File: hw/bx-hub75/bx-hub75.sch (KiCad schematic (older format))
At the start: 8 parts, among them U1 74HCT244, U2 74HCT244

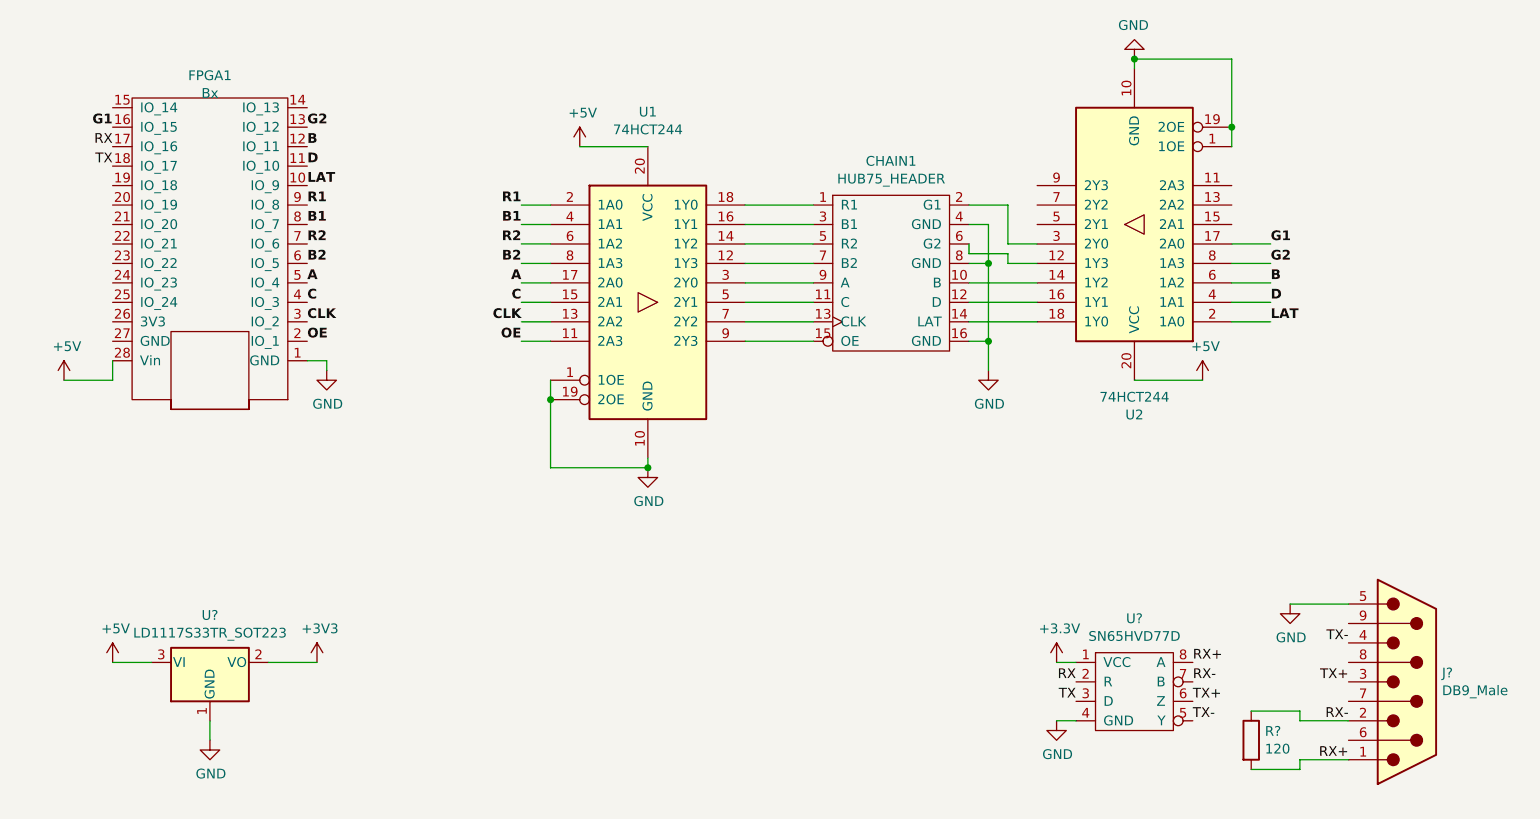
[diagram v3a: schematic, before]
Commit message: hw/bx-hub75: add SPI eeprom/decoupling caps
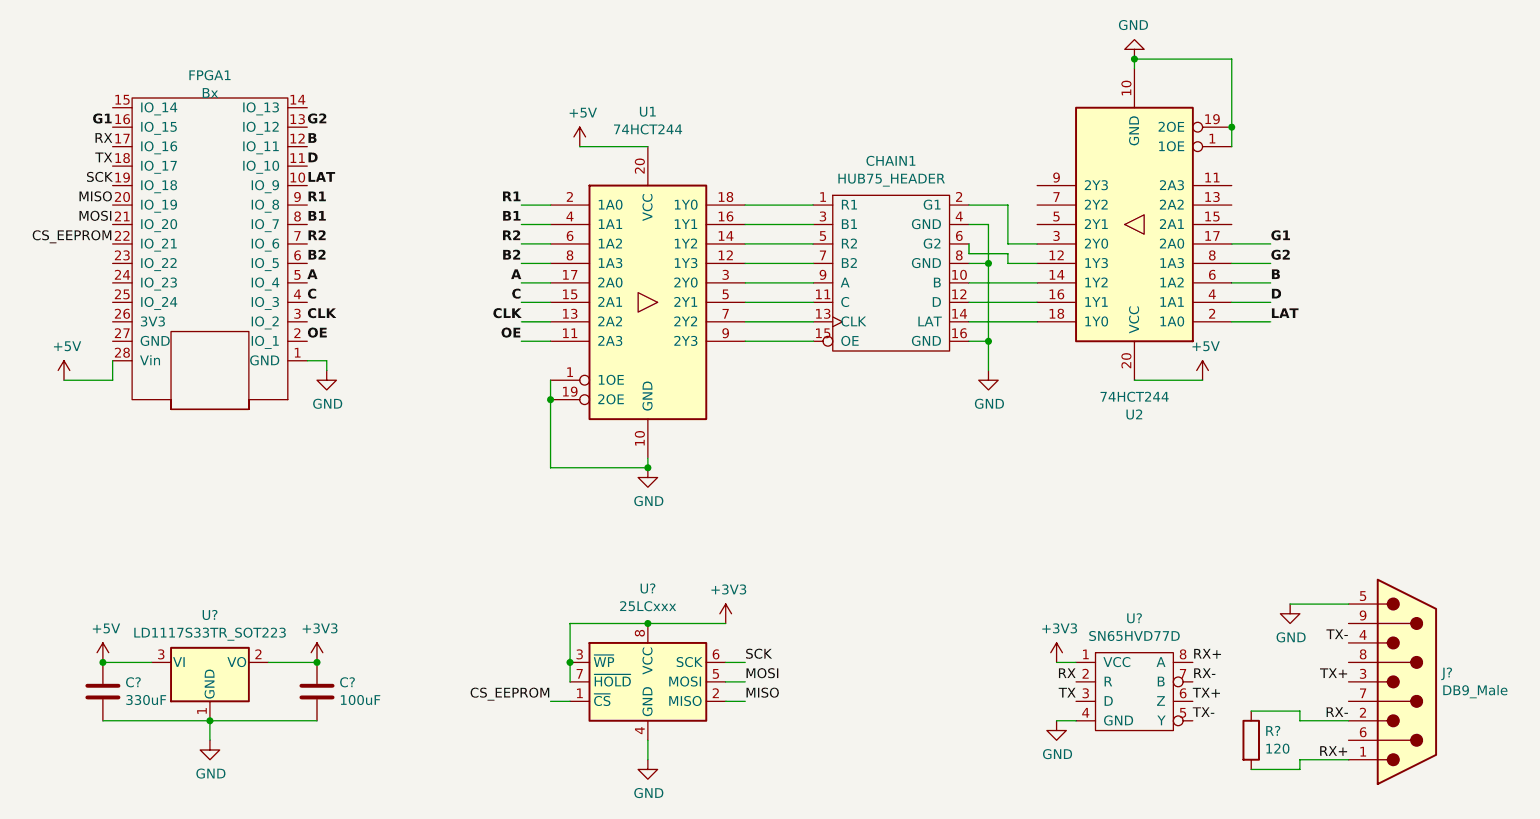
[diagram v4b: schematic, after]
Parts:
- added C?: 330uF, symbol Device:C
- added C?: 100uF, symbol Device:C
- added U?: 25LCxxx, symbol Memory_EEPROM:25LCxxx
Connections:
- net +3V3: now also C?.1, U?.3 (~WP), U?.7 (~HOLD), U?.8 (VCC)
- net +5V: now also C?.1
- net GND: now also C?.2, C?.2, U?.4 (GND)
- net SCK: now reaches FPGA1.19 (IO_18)
- net SCK: now also U?.6 (SCK)
- net MISO: now reaches FPGA1.20 (IO_19)
- net MISO: now also U?.2 (MISO)
- net MOSI: now reaches FPGA1.21 (IO_20)
- net MOSI: now also U?.5 (MOSI)
- net CS_EEPROM: now reaches FPGA1.22 (IO_21)
- net CS_EEPROM: now also U?.1 (~CS)
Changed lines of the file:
@@
-$EndComp
-$Comp
-L power:+3.3V #PWR?
-U 1 1 5BECFB36
-P 7200 5000
-F 0 "#PWR?" H 7200 4850 50  0001 C CNN
-F 1 "+3.3V" H 7215 5173 50  0000 C CNN
-F 2 "" H 7200 5000 50  0001 C CNN
-F 3 "" H 7200 5000 50  0001 C CNN
-	1    7200 5000
-	1    0    0    -1
 $EndComp
 $Comp
@@
 L power:+5V #PWR?
 U 1 1 5BEF2B74
-P 2350 5000
-F 0 "#PWR?" H 2350 4850 50  0001 C CNN
-F 1 "+5V" H 2365 5173 50  0000 C CNN
-F 2 "" H 2350 5000 50  0001 C CNN
-F 3 "" H 2350 5000 50  0001 C CNN
-	1    2350 5000
+P 2300 5000
+F 0 "#PWR?" H 2300 4850 50  0001 C CNN
+F 1 "+5V" H 2315 5173 50  0000 C CNN
+F 2 "" H 2300 5000 50  0001 C CNN
+F 3 "" H 2300 5000 50  0001 C CNN
+	1    2300 5000
 	1    0    0    -1
 $EndComp
@@
 	2850 5300 2850 5400
 Wire Wire Line
-	2550 5000 2350 5000
+	2550 5000 2300 5000
 $Comp
 L power:+3V3 #PWR?
@@
 Wire Wire Line
 	3400 5000 3150 5000
+$Comp
+L Memory_EEPROM:25LCxxx U?
+U 1 1 5BF300CE
+P 5100 5100
+F 0 "U?" H 5100 5578 50  0000 C CNN
+F 1 "25LCxxx" H 5100 5487 50  0000 C CNN
+F 2 "" H 5100 5100 50  0001 C CNN
+F 3 "http://ww1.microchip.com/downloads/en/DeviceDoc/21832H.pdf" H 5100 5100 50  0001 C CNN
+	1    5100 5100
+	1    0    0    -1
+$EndComp
+$Comp
+L power:GND #PWR?
+U 1 1 5BF30EFA
+P 5100 5500
+F 0 "#PWR?" H 5100 5250 50  0001 C CNN
+F 1 "GND" H 5105 5327 50  0000 C CNN
+F 2 "" H 5100 5500 50  0001 C CNN
+F 3 "" H 5100 5500 50  0001 C CNN
+	1    5100 5500
+	1    0    0    -1
+$EndComp
+Wire Wire Line
+	5100 5400 5100 5500
+$Comp
+L power:+3V3 #PWR?
+U 1 1 5BF3331A
+P 7200 5000
+F 0 "#PWR?" H 7200 4850 50  0001 C CNN
+F 1 "+3V3" H 7215 5173 50  0000 C CNN
+F 2 "" H 7200 5000 50  0001 C CNN
+F 3 "" H 7200 5000 50  0001 C CNN
+	1    7200 5000
+	1    0    0    -1
+$EndComp
+$Comp
+L power:+3V3 #PWR?
+U 1 1 5BF33357
+P 5500 4800
+F 0 "#PWR?" H 5500 4650 50  0001 C CNN
+F 1 "+3V3" H 5515 4973 50  0000 C CNN
+F 2 "" H 5500 4800 50  0001 C CNN
+F 3 "" H 5500 4800 50  0001 C CNN
+	1    5500 4800
+	1    0    0    -1
+$EndComp
+Wire Wire Line
+	5500 4800 5100 4800
+Text Label 4600 5200 2    50   ~ 0
+CS_EEPROM
+Wire Wire Line
+	4700 5200 4600 5200
+Text Label 5600 5000 0    50   ~ 0
+SCK
+Text Label 5600 5100 0    50   ~ 0
+MOSI
+Text Label 5600 5200 0    50   ~ 0
+MISO
+Wire Wire Line
+	5600 5200 5500 5200
+Wire Wire Line
+	5500 5100 5600 5100
+Wire Wire Line
+	5600 5000 5500 5000
+Wire Wire Line
+	4700 5000 4700 4800
+Wire Wire Line
+	4700 4800 5100 4800
+Connection ~ 5100 4800
+Wire Wire Line
+	4700 5100 4700 5000
+Connection ~ 4700 5000
+Text Label 2350 2550 2    50   ~ 0
+SCK
+Text Label 2350 2650 2    50   ~ 0
+MISO
+Text Label 2350 2750 2    50   ~ 0
+MOSI
+Text Label 2350 2850 2    50   ~ 0
+CS_EEPROM
+$Comp
+L Device:C C?
+U 1 1 5BF3FDFE
+P 2300 5150
+F 0 "C?" H 2415 5196 50  0000 L CNN
+F 1 "330uF" H 2415 5105 50  0000 L CNN
+F 2 "" H 2338 5000 50  0001 C CNN
+F 3 "~" H 2300 5150 50  0001 C CNN
+	1    2300 5150
+	1    0    0    -1
+$EndComp
+Connection ~ 2300 5000
+Wire Wire Line
+	2300 5300 2850 5300
+Connection ~ 2850 5300
+$Comp
+L Device:C C?
+U 1 1 5BF41834
+P 3400 5150
+F 0 "C?" H 3515 5196 50  0000 L CNN
+F 1 "100uF" H 3515 5105 50  0000 L CNN
+F 2 "" H 3438 5000 50  0001 C CNN
+F 3 "~" H 3400 5150 50  0001 C CNN
+	1    3400 5150
+	1    0    0    -1
+$EndComp
+Connection ~ 3400 5000
+Wire Wire Line
+	3400 5300 2850 5300
 $EndSCHEMATC

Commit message: hw/bx-hub75: Initial PCB layout.
God, routing this is complex.
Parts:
- C1: renamed from C?; footprint (none) -> Capacitor_SMD:CP_Elec_6.3x7.7
- C2: renamed from C?; footprint (none) -> Capacitor_SMD:CP_Elec_5x5.4
- CHAIN1: footprint (none) -> Random:HUB75_HEADER
- FPGA1: footprint (none) -> TinyFPGA:TinyFPGA_BX
- J1: renamed from J?; footprint (none) -> Connector_Dsub:DSUB-9_Male_Horizontal_P2.77x2.84mm_EdgePinOffset4.94mm_Housed_MountingHolesOffset7.48mm
- R1: renamed from R?; footprint (none) -> Resistor_SMD:R_1210_3225Metric_Pad1.42x2.65mm_HandSolder
- U1, U2: footprint (none) -> Package_SO:SO-20_12.8x7.5mm_P1.27mm
- U4, U5: renamed from U?; footprint (none) -> Package_SO:SOIC-8_3.9x4.9mm_P1.27mm
- gave numbers to parts that had none: 1
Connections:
- net RX+: now also J1.2, R1.1; no longer J1.1, R1.2
- net RX-: now also J1.1, R1.2; no longer J1.2, R1.1
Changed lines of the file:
@@
 F 0 "FPGA1" H 2850 1985 50  0000 C CNN
 F 1 "Bx" H 2850 2076 50  0000 C CNN
-F 2 "" H 3000 3550 50  0001 C CNN
+F 2 "TinyFPGA:TinyFPGA_BX" H 3000 3550 50  0001 C CNN
 F 3 "" H 3000 3550 50  0001 C CNN
 	1    2850 2850
@@
 F 0 "CHAIN1" H 6350 3575 50  0000 C CNN
 F 1 "HUB75_HEADER" H 6350 3484 50  0000 C CNN
-F 2 "" H 6350 2550 50  0001 C CNN
+F 2 "Random:HUB75_HEADER" H 6350 2550 50  0001 C CNN
 F 3 "" H 6350 2550 50  0001 C CNN
 	1    6350 3000
@@
 F 0 "U1" H 5100 4128 50  0000 C CNN
 F 1 "74HCT244" H 5100 4037 50  0000 C CNN
-F 2 "" H 5100 3150 50  0001 C CNN
+F 2 "Package_SO:SO-20_12.8x7.5mm_P1.27mm" H 5100 3150 50  0001 C CNN
 F 3 "http://www.nxp.com/documents/data_sheet/74HC_HCT244.pdf" H 5100 3150 50  0001 C CNN
 	1    5100 3150
@@
 F 0 "U2" H 7600 3728 50  0000 C CNN
 F 1 "74HCT244" H 7600 3637 50  0000 C CNN
-F 2 "" H 7600 2750 50  0001 C CNN
+F 2 "Package_SO:SO-20_12.8x7.5mm_P1.27mm" H 7600 2750 50  0001 C CNN
 F 3 "http://www.nxp.com/documents/data_sheet/74HC_HCT244.pdf" H 7600 2750 50  0001 C CNN
 	1    7600 2750
@@
 	5950 3350 5600 3350
 $Comp
-L power:+5V #PWR?
+L power:+5V #PWR0106
 U 1 1 5BEDB440
 P 4750 2350
-F 0 "#PWR?" H 4750 2200 50  0001 C CNN
+F 0 "#PWR0106" H 4750 2200 50  0001 C CNN
 F 1 "+5V" H 4765 2523 50  0000 C CNN
 F 2 "" H 4750 2350 50  0001 C CNN
@@
 $EndComp
 $Comp
-L power:+5V #PWR?
+L power:+5V #PWR0107
 U 1 1 5BEDB676
 P 7950 3550
-F 0 "#PWR?" H 7950 3400 50  0001 C CNN
+F 0 "#PWR0107" H 7950 3400 50  0001 C CNN
 F 1 "+5V" H 7965 3723 50  0000 C CNN
 F 2 "" H 7950 3550 50  0001 C CNN
@@
 G1
 $Comp
-L Random:SN65HVD77D U?
+L Random:SN65HVD77D U5
 U 1 1 5BECF5D6
 P 7600 5150
-F 0 "U?" H 7600 5525 50  0000 C CNN
+F 0 "U5" H 7600 5525 50  0000 C CNN
 F 1 "SN65HVD77D" H 7600 5434 50  0000 C CNN
-F 2 "" H 7600 4900 50  0001 C CNN
+F 2 "Package_SO:SOIC-8_3.9x4.9mm_P1.27mm" H 7600 4900 50  0001 C CNN
 F 3 "" H 7600 4900 50  0001 C CNN
 	1    7600 5150
@@
 $EndComp
 $Comp
-L power:GND #PWR?
+L power:GND #PWR0108
 U 1 1 5BECFBC2
 P 7200 5300
-F 0 "#PWR?" H 7200 5050 50  0001 C CNN
+F 0 "#PWR0108" H 7200 5050 50  0001 C CNN
 F 1 "GND" H 7205 5127 50  0000 C CNN
 F 2 "" H 7200 5300 50  0001 C CNN
@@
 TX
 $Comp
-L Connector:DB9_Male J?
+L Connector:DB9_Male J1
 U 1 1 5BED180D
 P 9000 5100
-F 0 "J?" H 9180 5146 50  0000 L CNN
+F 0 "J1" H 9180 5146 50  0000 L CNN
 F 1 "DB9_Male" H 9180 5055 50  0000 L CNN
-F 2 "" H 9000 5100 50  0001 C CNN
+F 2 "Connector_Dsub:DSUB-9_Male_Horizontal_P2.77x2.84mm_EdgePinOffset4.94mm_Housed_MountingHolesOffset7.48mm" H 9000 5100 50  0001 C CNN
 F 3 " ~" H 9000 5100 50  0001 C CNN
 	1    9000 5100
@@
 TX-
 Text Label 8700 5500 2    50   ~ 0
+RX-
+Text Label 8700 5300 2    50   ~ 0
 RX+
-Text Label 8700 5300 2    50   ~ 0
-RX-
 Text Label 8700 5100 2    50   ~ 0
 TX+
@@
 TX-
 $Comp
-L power:GND #PWR?
+L power:GND #PWR0109
 U 1 1 5BEDE34B
 P 8400 4700
-F 0 "#PWR?" H 8400 4450 50  0001 C CNN
+F 0 "#PWR0109" H 8400 4450 50  0001 C CNN
 F 1 "GND" H 8405 4527 50  0000 C CNN
 F 2 "" H 8400 4700 50  0001 C CNN
@@
 	8400 4700 8700 4700
 $Comp
-L Device:R R?
+L Device:R R1
 U 1 1 5BEE0AE3
 P 8200 5400
-F 0 "R?" H 8270 5446 50  0000 L CNN
+F 0 "R1" H 8270 5446 50  0000 L CNN
 F 1 "120" H 8270 5355 50  0000 L CNN
-F 2 "" V 8130 5400 50  0001 C CNN
+F 2 "Resistor_SMD:R_1210_3225Metric_Pad1.42x2.65mm_HandSolder" V 8130 5400 50  0001 C CNN
 F 3 "~" H 8200 5400 50  0001 C CNN
 	1    8200 5400
@@
 TX
 $Comp
-L Regulator_Linear:LD1117S33TR_SOT223 U?
+L Regulator_Linear:LD1117S33TR_SOT223 U3
 U 1 1 5BEF264A
 P 2850 5000
-F 0 "U?" H 2850 5242 50  0000 C CNN
+F 0 "U3" H 2850 5242 50  0000 C CNN
 F 1 "LD1117S33TR_SOT223" H 2850 5151 50  0000 C CNN
 F 2 "Package_TO_SOT_SMD:SOT-223-3_TabPin2" H 2850 5200 50  0001 C CNN
@@
 $EndComp
 $Comp
-L power:+5V #PWR?
+L power:+5V #PWR0110
 U 1 1 5BEF2B74
 P 2300 5000
-F 0 "#PWR?" H 2300 4850 50  0001 C CNN
+F 0 "#PWR0110" H 2300 4850 50  0001 C CNN
 F 1 "+5V" H 2315 5173 50  0000 C CNN
 F 2 "" H 2300 5000 50  0001 C CNN
@@
 $EndComp
 $Comp
-L power:GND #PWR?
+L power:GND #PWR0111
 U 1 1 5BEF2BC3
 P 2850 5400
-F 0 "#PWR?" H 2850 5150 50  0001 C CNN
+F 0 "#PWR0111" H 2850 5150 50  0001 C CNN
 F 1 "GND" H 2855 5227 50  0000 C CNN
 F 2 "" H 2850 5400 50  0001 C CNN
@@
 	2550 5000 2300 5000
 $Comp
-L power:+3V3 #PWR?
+L power:+3V3 #PWR0112
 U 1 1 5BEF8C03
 P 3400 5000
-F 0 "#PWR?" H 3400 4850 50  0001 C CNN
+F 0 "#PWR0112" H 3400 4850 50  0001 C CNN
 F 1 "+3V3" H 3415 5173 50  0000 C CNN
 F 2 "" H 3400 5000 50  0001 C CNN
@@
 	3400 5000 3150 5000
 $Comp
-L Memory_EEPROM:25LCxxx U?
+L Memory_EEPROM:25LCxxx U4
 U 1 1 5BF300CE
 P 5100 5100
-F 0 "U?" H 5100 5578 50  0000 C CNN
+F 0 "U4" H 5100 5578 50  0000 C CNN
 F 1 "25LCxxx" H 5100 5487 50  0000 C CNN
-F 2 "" H 5100 5100 50  0001 C CNN
+F 2 "Package_SO:SOIC-8_3.9x4.9mm_P1.27mm" H 5100 5100 50  0001 C CNN
 F 3 "http://ww1.microchip.com/downloads/en/DeviceDoc/21832H.pdf" H 5100 5100 50  0001 C CNN
 	1    5100 5100
@@
 $EndComp
 $Comp
-L power:GND #PWR?
+L power:GND #PWR0113
 U 1 1 5BF30EFA
 P 5100 5500
-F 0 "#PWR?" H 5100 5250 50  0001 C CNN
+F 0 "#PWR0113" H 5100 5250 50  0001 C CNN
 F 1 "GND" H 5105 5327 50  0000 C CNN
 F 2 "" H 5100 5500 50  0001 C CNN
@@
 	5100 5400 5100 5500
 $Comp
-L power:+3V3 #PWR?
+L power:+3V3 #PWR0114
 U 1 1 5BF3331A
 P 7200 5000
-F 0 "#PWR?" H 7200 4850 50  0001 C CNN
+F 0 "#PWR0114" H 7200 4850 50  0001 C CNN
 F 1 "+3V3" H 7215 5173 50  0000 C CNN
 F 2 "" H 7200 5000 50  0001 C CNN
@@
 $EndComp
 $Comp
-L power:+3V3 #PWR?
+L power:+3V3 #PWR0115
 U 1 1 5BF33357
 P 5500 4800
-F 0 "#PWR?" H 5500 4650 50  0001 C CNN
+F 0 "#PWR0115" H 5500 4650 50  0001 C CNN
 F 1 "+3V3" H 5515 4973 50  0000 C CNN
 F 2 "" H 5500 4800 50  0001 C CNN
@@
 CS_EEPROM
 $Comp
-L Device:C C?
+L Device:C C1
 U 1 1 5BF3FDFE
 P 2300 5150
-F 0 "C?" H 2415 5196 50  0000 L CNN
+F 0 "C1" H 2415 5196 50  0000 L CNN
 F 1 "330uF" H 2415 5105 50  0000 L CNN
-F 2 "" H 2338 5000 50  0001 C CNN
+F 2 "Capacitor_SMD:CP_Elec_6.3x7.7" H 2338 5000 50  0001 C CNN
 F 3 "~" H 2300 5150 50  0001 C CNN
 	1    2300 5150
@@
 Connection ~ 2850 5300
 $Comp
-L Device:C C?
+L Device:C C2
 U 1 1 5BF41834
 P 3400 5150
-F 0 "C?" H 3515 5196 50  0000 L CNN
+F 0 "C2" H 3515 5196 50  0000 L CNN
 F 1 "100uF" H 3515 5105 50  0000 L CNN
-F 2 "" H 3438 5000 50  0001 C CNN
+F 2 "Capacitor_SMD:CP_Elec_5x5.4" H 3438 5000 50  0001 C CNN
 F 3 "~" H 3400 5150 50  0001 C CNN
 	1    3400 5150

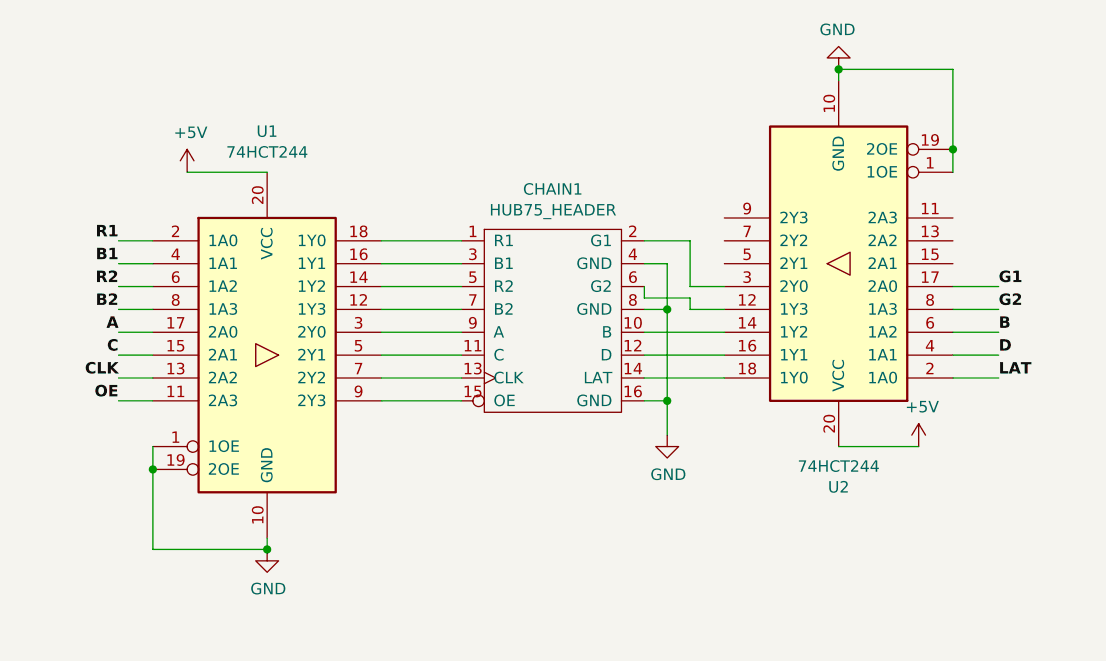
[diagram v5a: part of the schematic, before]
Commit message: hw/bx-hub75: 74HCT244 -> 74HCT541
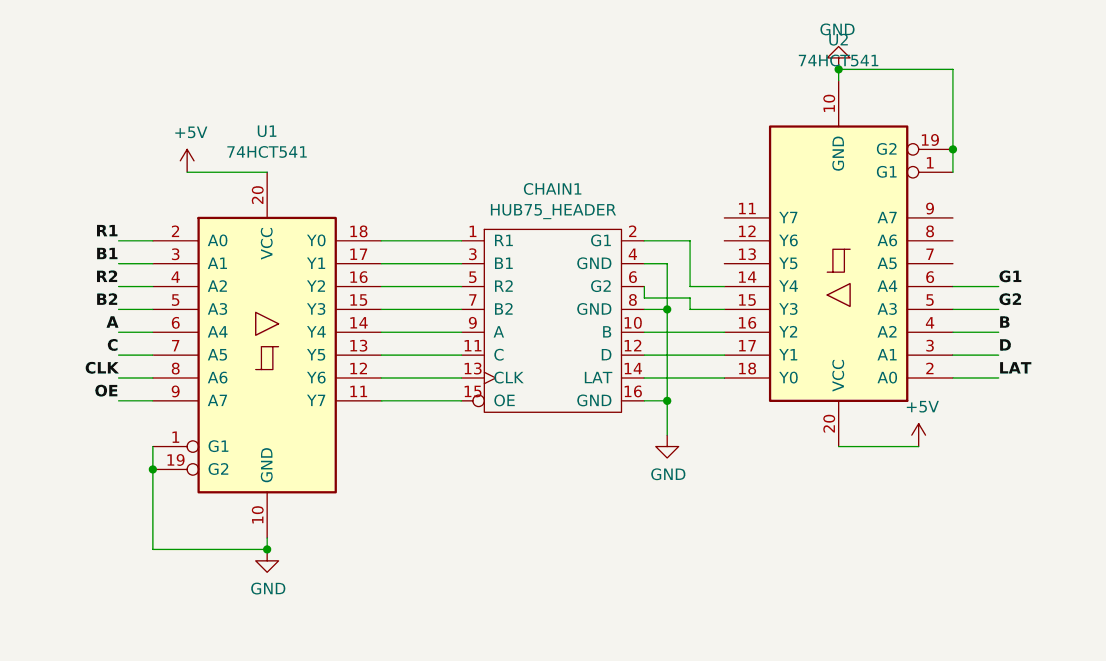
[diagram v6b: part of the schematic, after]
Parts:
- removed U1, U2: 74HCT244, Package_SO:SO-20_12.8x7.5mm_P1.27mm, symbol 74xx:74HCT244
- added U1, U2: 74HCT541, Package_SO:SOIC-20W_7.5x12.8mm_P1.27mm, symbol 74xx:74HCT541
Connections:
- net +5V: now also U1.20 (VCC), U2.20 (VCC)
- net A: now also U1.6 (A4)
- net B: now also U2.4 (A2)
- net B1: now also U1.3 (A1)
- net B2: now also U1.5 (A3)
- net C: now also U1.7 (A5)
- net CLK: now also U1.8 (A6)
- net D: now also U2.3 (A1)
- net G1: now also U2.6 (A4)
- net G2: now also U2.5 (A3)
- net GND: now also U1.1 (G1), U1.10 (GND), U1.19 (G2), U2.1 (G1), U2.10 (GND), U2.19 (G2)
- net LAT: now also U2.2 (A0)
- net OE: now also U1.9 (A7)
- net R1: now also U1.2 (A0)
- net R2: now also U1.4 (A2)
- net at CHAIN1.1 (R1): now also U1.18 (Y0)
- net at CHAIN1.10 (B): now also U2.16 (Y2)
- net at CHAIN1.11 (C): now also U1.13 (Y5)
- net at CHAIN1.12 (D): now also U2.17 (Y1)
- net at CHAIN1.13 (CLK): now also U1.12 (Y6)
- net at CHAIN1.14 (LAT): now also U2.18 (Y0)
- net at CHAIN1.15 (OE): now also U1.11 (Y7)
- net at CHAIN1.2 (G1): now also U2.14 (Y4)
- net at CHAIN1.3 (B1): now also U1.17 (Y1)
- net at CHAIN1.5 (R2): now also U1.16 (Y2)
- net at CHAIN1.6 (G2): now also U2.15 (Y3)
- net at CHAIN1.7 (B2): now also U1.15 (Y3)
- net at CHAIN1.9 (A): now also U1.14 (Y4)
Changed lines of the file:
@@
-$EndComp
-$Comp
-L 74xx:74HCT244 U1
-U 1 1 5BECA77E
-P 5100 3150
-F 0 "U1" H 5100 4128 50  0000 C CNN
-F 1 "74HCT244" H 5100 4037 50  0000 C CNN
-F 2 "Package_SO:SO-20_12.8x7.5mm_P1.27mm" H 5100 3150 50  0001 C CNN
-F 3 "http://www.nxp.com/documents/data_sheet/74HC_HCT244.pdf" H 5100 3150 50  0001 C CNN
-	1    5100 3150
-	1    0    0    -1
-$EndComp
-$Comp
-L 74xx:74HCT244 U2
-U 1 1 5BECA862
-P 7600 2750
-F 0 "U2" H 7600 3728 50  0000 C CNN
-F 1 "74HCT244" H 7600 3637 50  0000 C CNN
-F 2 "Package_SO:SO-20_12.8x7.5mm_P1.27mm" H 7600 2750 50  0001 C CNN
-F 3 "http://www.nxp.com/documents/data_sheet/74HC_HCT244.pdf" H 7600 2750 50  0001 C CNN
-	1    7600 2750
-	-1   0    0    1
 $EndComp
 $Comp
@@
 $EndComp
 Wire Wire Line
-	4600 3550 4600 3650
-Connection ~ 4600 3650
-Wire Wire Line
 	7600 1950 7600 1900
 $Comp
@@
 	5100 2350 4750 2350
 Wire Wire Line
-	8100 2350 8100 2250
-Wire Wire Line
 	8100 2250 8100 1900
 Wire Wire Line
 	8100 1900 7600 1900
-Connection ~ 8100 2250
 Connection ~ 7600 1900
 Text Label 4450 2650 2    50   ~ 10
@@
 Wire Wire Line
 	3400 5300 2850 5300
+$Comp
+L 74xx:74HCT541 U1
+U 1 1 5BF5EC63
+P 5100 3150
+F 0 "U1" H 5100 4128 50  0000 C CNN
+F 1 "74HCT541" H 5100 4037 50  0000 C CNN
+F 2 "Package_SO:SOIC-20W_7.5x12.8mm_P1.27mm" H 5100 3150 50  0001 C CNN
+F 3 "http://www.ti.com/lit/gpn/sn74HCT541" H 5100 3150 50  0001 C CNN
+	1    5100 3150
+	1    0    0    -1
+$EndComp
+Wire Wire Line
+	4600 3550 4600 3650
+Connection ~ 4600 3650
+$Comp
+L 74xx:74HCT541 U2
+U 1 1 5BF6300B
+P 7600 2750
+F 0 "U2" H 7600 1772 50  0000 C CNN
+F 1 "74HCT541" H 7600 1863 50  0000 C CNN
+F 2 "Package_SO:SOIC-20W_7.5x12.8mm_P1.27mm" H 7600 2750 50  0001 C CNN
+F 3 "http://www.ti.com/lit/gpn/sn74HCT541" H 7600 2750 50  0001 C CNN
+	1    7600 2750
+	-1   0    0    1
+$EndComp
+Wire Wire Line
+	8100 2350 8100 2250
+Connection ~ 8100 2250
 $EndSCHEMATC
